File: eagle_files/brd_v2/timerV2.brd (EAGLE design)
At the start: 99.4 x 39.2 mm, 42 parts, among them IC6 DS1307, U1 ATMEGA328P

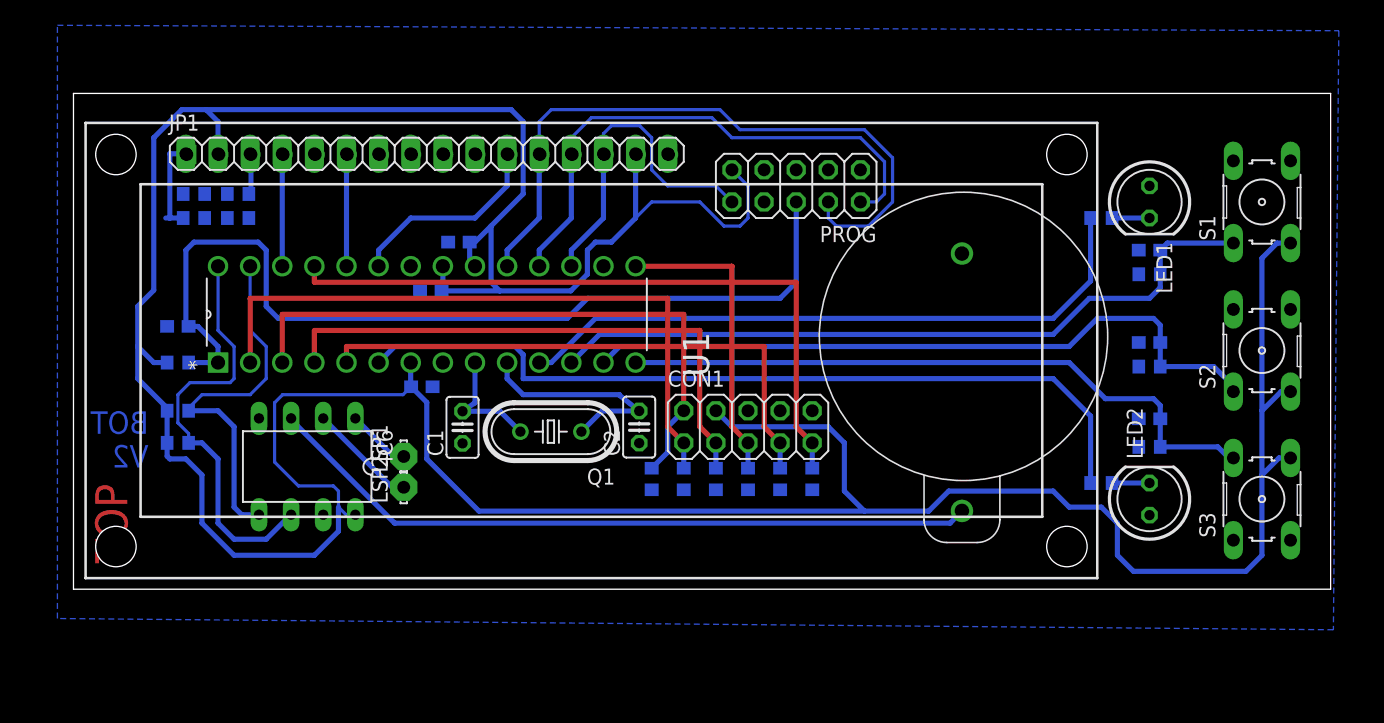
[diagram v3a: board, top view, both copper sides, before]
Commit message: added pullup resistors ...
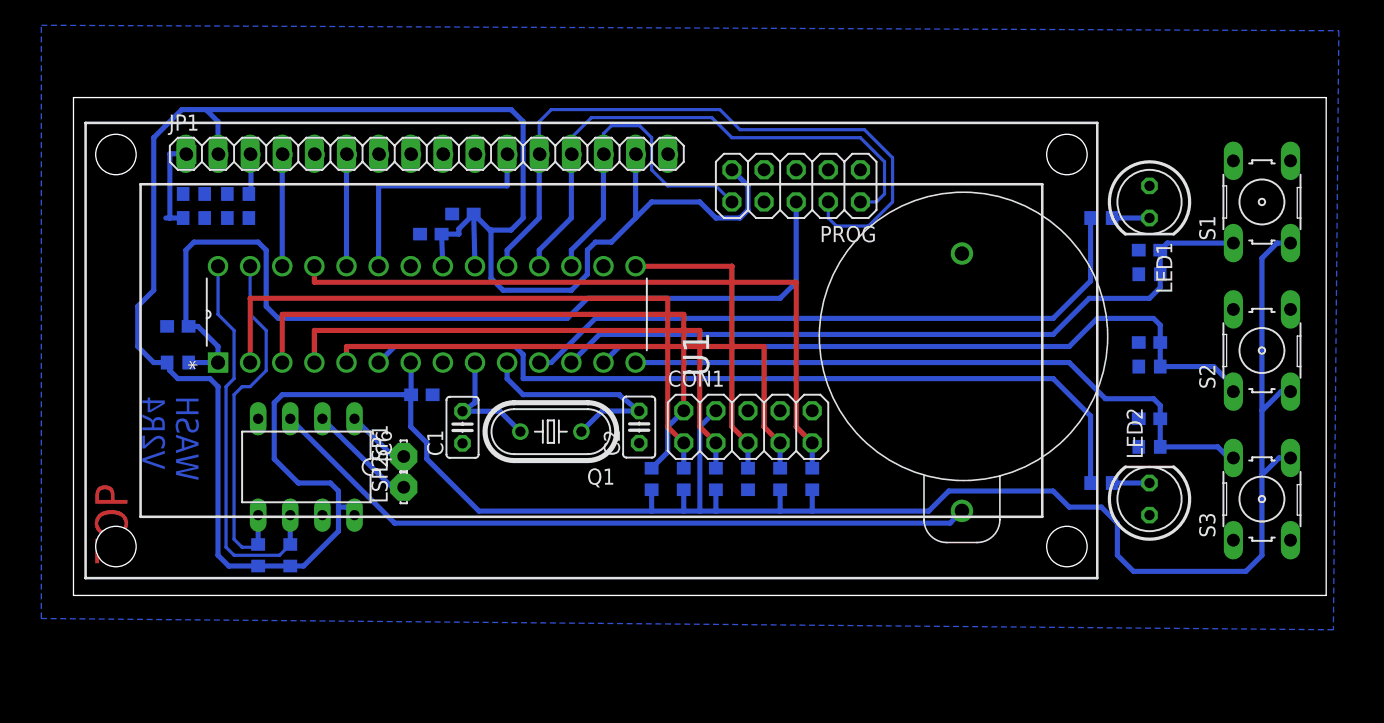
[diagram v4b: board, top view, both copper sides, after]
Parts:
- moved R2 13.1 mm to (15.9, 6.35), turned to 90 degrees
- moved R20 12.6 mm to (18.4, 6.35), turned to 90 degrees
- moved C10 4.45 mm to (29.5, 31.8)
- moved C4 2.25 mm to (32.1, 33.3)
- moved C5 0.63 mm to (28.8, 19.0)
- moved IC6 0.07 mm to (19.7, 13.3)
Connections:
- net GND: no longer R14.2, R15.2, R16.2, R7.2, R9.2
- net VCC: now also R14.2, R15.2, R16.2, R7.2, R9.2
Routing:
- net DB4: track 16.2 -> 19.1 mm
- net N$39: track 33.6 -> 31.1 mm
- net N$40: track 29.4 -> 28.1 mm
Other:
- board size 99.4 x 39.2 mm -> 99.1 x 39.4 mm
- board text added: "WASH V2R4"
- board text removed: "BOT V2"

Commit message: changed layout
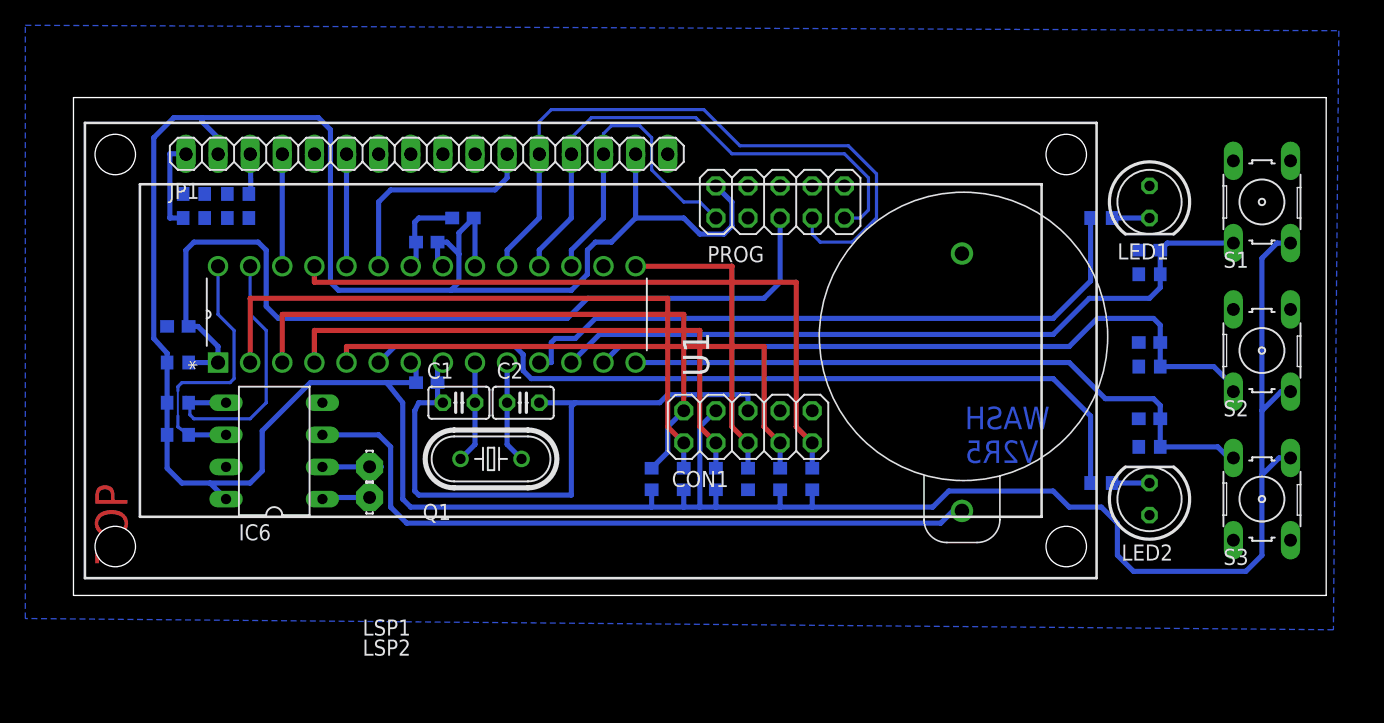
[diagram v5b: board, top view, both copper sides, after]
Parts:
- R14, R15, R16, R17, R7, R9: value 105 -> 10k
- moved R2 13.6 mm to (9.53, 18.4), turned to 180 degrees
- moved R20 13.0 mm to (9.53, 15.9), turned to 180 degrees
- moved C2 9.37 mm to (36.8, 18.4), turned to 180 degrees
- moved Q1 5.20 mm to (34.3, 14.0)
- moved LSP1 4.22 mm to (24.7, 10.9), turned to 270 degrees
- moved LSP2 3.15 mm to (24.7, 13.4), turned to 270 degrees
- moved IC6 2.84 mm to (17.1, 14.6), turned to 90 degrees
- moved C1 1.97 mm to (31.8, 18.4), turned to 0 degrees
- moved PROG 1.80 mm to (57.1, 34.3)
- moved C5 1.04 mm to (29.2, 20.0)
- moved C10 0.71 mm to (29.2, 31.1)
- moved C4 0.32 mm to (32.1, 33.0)
- moved U$2 0.05 mm to (42.2, 22.5)
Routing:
- net GND: track 7.72 -> 64.7 mm
- net VCC: track 301.0 -> 276.1 mm
- net N$46: track 18.0 -> 8.09 mm
- net N$39: track 31.1 -> 21.4 mm
- net N$40: track 28.1 -> 22.4 mm
- net N$33: track 8.65 -> 5.57 mm
- net N$5: track 73.9 -> 71.3 mm
- net N$44: track 9.61 -> 8.09 mm
- net DB4: track 19.1 -> 17.9 mm
- net N$13: track 51.3 -> 52.2 mm
- net DB7: track 26.0 -> 25.3 mm
- net DB6: track 42.9 -> 42.1 mm
- net DB5: track 53.4 -> 52.7 mm
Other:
- board text added: "WASH V2R5"
- board text removed: "WASH V2R4"

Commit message: Schematic cleaned up
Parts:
- moved LSP1 2.54 mm to (24.7, 8.38)
- moved LSP2 2.54 mm to (24.7, 10.8)
- moved R10 0.71 mm to (11.4, 33.3)
- moved R12 0.71 mm to (11.4, 34.6), turned to 0 degrees
- moved C1 0.63 mm to (31.8, 17.8)
- moved C2 0.63 mm to (36.8, 17.8)
- moved C5 0.32 mm to (29.2, 19.7)
- moved R11 0.32 mm to (14.3, 33.3)
- moved R13 0.32 mm to (14.3, 34.6)
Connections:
- net N$3 renamed POWER_SWITCH
- new net N$10: JP1.7, U$2.7
- new net N$16: JP1.8, U$2.8
- new net N$18: JP1.9, U$2.9
- new net N$19: JP1.10, U$2.10
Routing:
- net VCC: track 276.1 -> 280.6 mm
- net N$33: track 5.57 -> 4.77 mm
